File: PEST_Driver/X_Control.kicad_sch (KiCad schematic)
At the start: 72 parts, among them J1 Conn_01x02, J2 Conn_01x02, J3 Conn_01x02, J4 Conn_01x02, J5 Conn_01x02, J6 Conn_01x02, J7 Conn_01x02, J8 Conn_01x02, U19 74HC4051, U2 74HC4051, U20 74HC4051, U21 74HC595, U22 74HC4051, U3 74HC4051

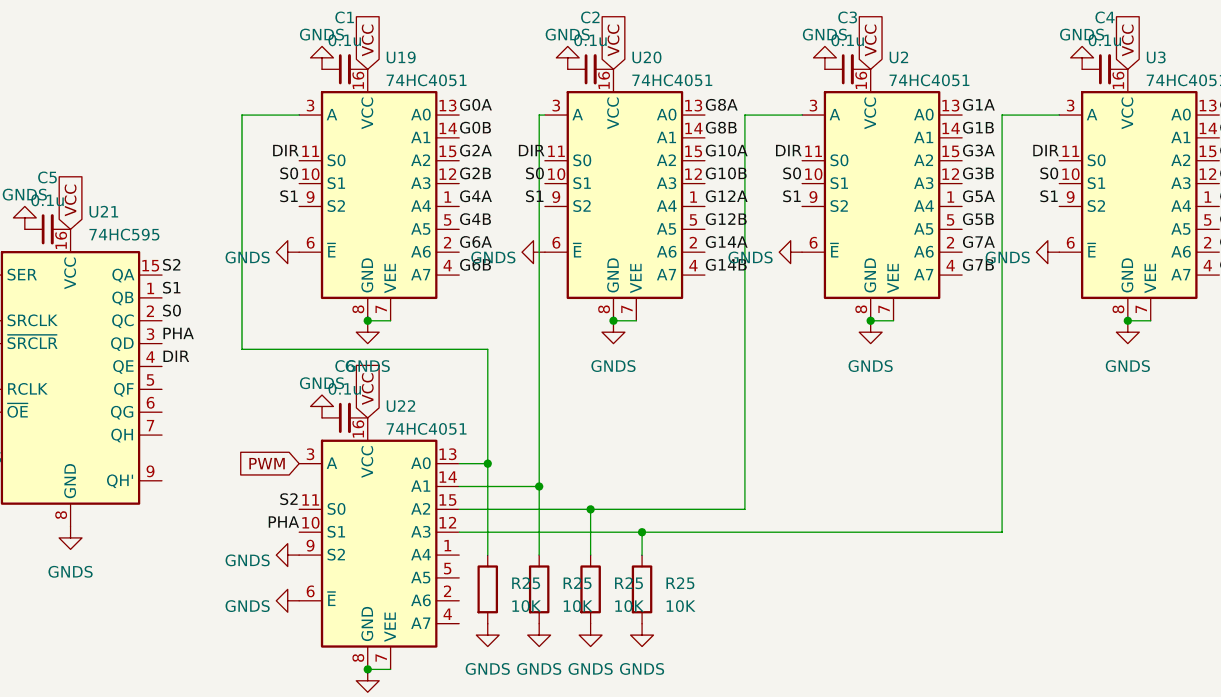
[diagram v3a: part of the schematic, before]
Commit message: Created basic DRIFT bus schematic and fixed PEST driver numbering
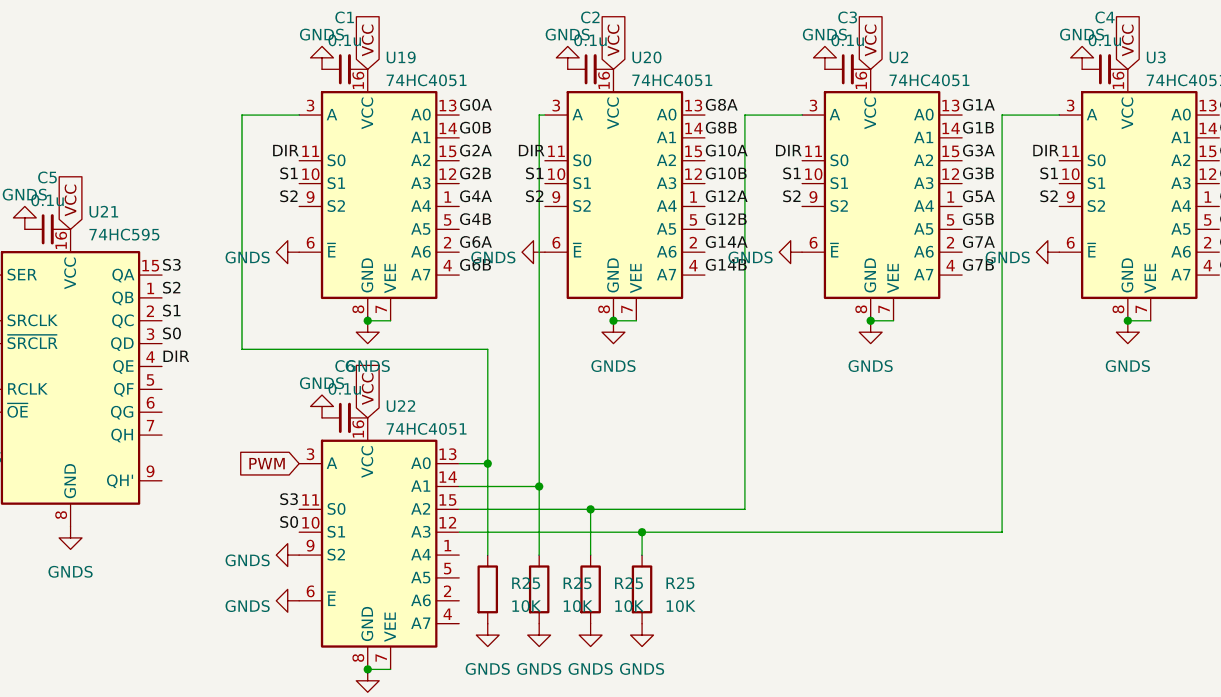
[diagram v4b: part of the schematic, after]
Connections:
- net PHA is gone; now on net S0: U21.3 (QD), U22.10 (S1)
- net S0: no longer U19.10 (S1), U2.10 (S1), U20.10 (S1), U21.2 (QC), U3.10 (S1)
- net S1: now also U19.10 (S1), U2.10 (S1), U20.10 (S1), U21.2 (QC), U3.10 (S1); no longer U19.9 (S2), U2.9 (S2), U20.9 (S2), U21.1 (QB), U3.9 (S2)
- net S2: now also U19.9 (S2), U2.9 (S2), U20.9 (S2), U21.1 (QB), U3.9 (S2); no longer U21.15 (QA), U22.11 (S0)
- new net S3: U21.15 (QA), U22.11 (S0)
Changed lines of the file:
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@@
     (effects (font (size 1.27 1.27)) (justify right bottom))
   )
-  (label "S1" (at 115.57 113.665 180) (fields_autoplaced)
+  (label "S2" (at 115.57 113.665 180) (fields_autoplaced)
     (effects (font (size 1.27 1.27)) (justify right bottom))
   )
@@
     (effects (font (size 1.27 1.27)) (justify left bottom))
   )
-  (label "S0" (at 59.69 111.125 180) (fields_autoplaced)
+  (label "S1" (at 59.69 111.125 180) (fields_autoplaced)
     (effects (font (size 1.27 1.27)) (justify right bottom))
   )
@@
     (effects (font (size 1.27 1.27)) (justify left bottom))
   )
-  (label "S1" (at 44.45 123.825 0) (fields_autoplaced)
+  (label "S2" (at 44.45 123.825 0) (fields_autoplaced)
     (effects (font (size 1.27 1.27)) (justify left bottom))
   )
@@
     (effects (font (size 1.27 1.27)) (justify left bottom))
   )
-  (label "S0" (at 44.45 126.365 0) (fields_autoplaced)
+  (label "S1" (at 44.45 126.365 0) (fields_autoplaced)
     (effects (font (size 1.27 1.27)) (justify left bottom))
   )
@@
     (effects (font (size 1.27 1.27)) (justify left bottom))
   )
-  (label "S1" (at 86.995 113.665 180) (fields_autoplaced)
+  (label "S2" (at 86.995 113.665 180) (fields_autoplaced)
     (effects (font (size 1.27 1.27)) (justify right bottom))
   )
@@
     (effects (font (size 1.27 1.27)) (justify left bottom))
   )
-  (label "S1" (at 59.69 113.665 180) (fields_autoplaced)
+  (label "S2" (at 59.69 113.665 180) (fields_autoplaced)
     (effects (font (size 1.27 1.27)) (justify right bottom))
   )
@@
     (effects (font (size 1.27 1.27)) (justify left bottom))
   )
-  (label "S0" (at 144.145 111.125 180) (fields_autoplaced)
+  (label "S1" (at 144.145 111.125 180) (fields_autoplaced)
     (effects (font (size 1.27 1.27)) (justify right bottom))
   )
@@
     (effects (font (size 1.27 1.27)) (justify left bottom))
   )
-  (label "S0" (at 86.995 111.125 180) (fields_autoplaced)
+  (label "S1" (at 86.995 111.125 180) (fields_autoplaced)
     (effects (font (size 1.27 1.27)) (justify right bottom))
   )
@@
     (effects (font (size 1.27 1.27)) (justify left bottom))
   )
-  (label "S1" (at 144.145 113.665 180) (fields_autoplaced)
+  (label "S2" (at 144.145 113.665 180) (fields_autoplaced)
     (effects (font (size 1.27 1.27)) (justify right bottom))
   )
@@
     (effects (font (size 1.27 1.27)) (justify left bottom))
   )
-  (label "PHA" (at 59.69 149.86 180) (fields_autoplaced)
+  (label "S0" (at 59.69 149.86 180) (fields_autoplaced)
     (effects (font (size 1.27 1.27)) (justify right bottom))
   )
@@
     (effects (font (size 1.27 1.27)) (justify left bottom))
   )
-  (label "S2" (at 59.69 147.32 180) (fields_autoplaced)
+  (label "S3" (at 59.69 147.32 180) (fields_autoplaced)
     (effects (font (size 1.27 1.27)) (justify right bottom))
   )
@@
     (effects (font (size 1.27 1.27)) (justify left bottom))
   )
-  (label "S2" (at 44.45 121.285 0) (fields_autoplaced)
+  (label "S3" (at 44.45 121.285 0) (fields_autoplaced)
     (effects (font (size 1.27 1.27)) (justify left bottom))
   )
@@
     (effects (font (size 1.27 1.27)) (justify right bottom))
   )
-  (label "S0" (at 115.57 111.125 180) (fields_autoplaced)
+  (label "S1" (at 115.57 111.125 180) (fields_autoplaced)
     (effects (font (size 1.27 1.27)) (justify right bottom))
   )
@@
     (effects (font (size 1.27 1.27)) (justify left bottom))
   )
-  (label "PHA" (at 44.45 128.905 0) (fields_autoplaced)
-    (effects (font (size 1.27 1.27)) (justify left bottom))
-  )
+  (label "S0" (at 44.45 128.905 0) (fields_autoplaced)
+    (effects (font (size 1.27 1.27)) (justify left bottom))
+  )
